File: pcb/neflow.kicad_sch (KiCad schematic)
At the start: 62 parts, among them J101 1333870, J102 FAN0, J103 SSR0, J104 FAN1, J105 SSR1, J106 Temp0, J107 Temp1, Q101 Q_PMOS_GSD, Q102 IRLML2502, Q103 IRLML2502, Q104 IRLML2502, Q105 IRLML2502, Q106 IRLML2502, SW101 SW_Push, SW102 SW_Push, SW103 SW_Push, SW104 SW_Push, U101 Pico, U102 TLV803EF29DBZR, U103 MAX31855KASA+T, U104 MAX31855KASA+T

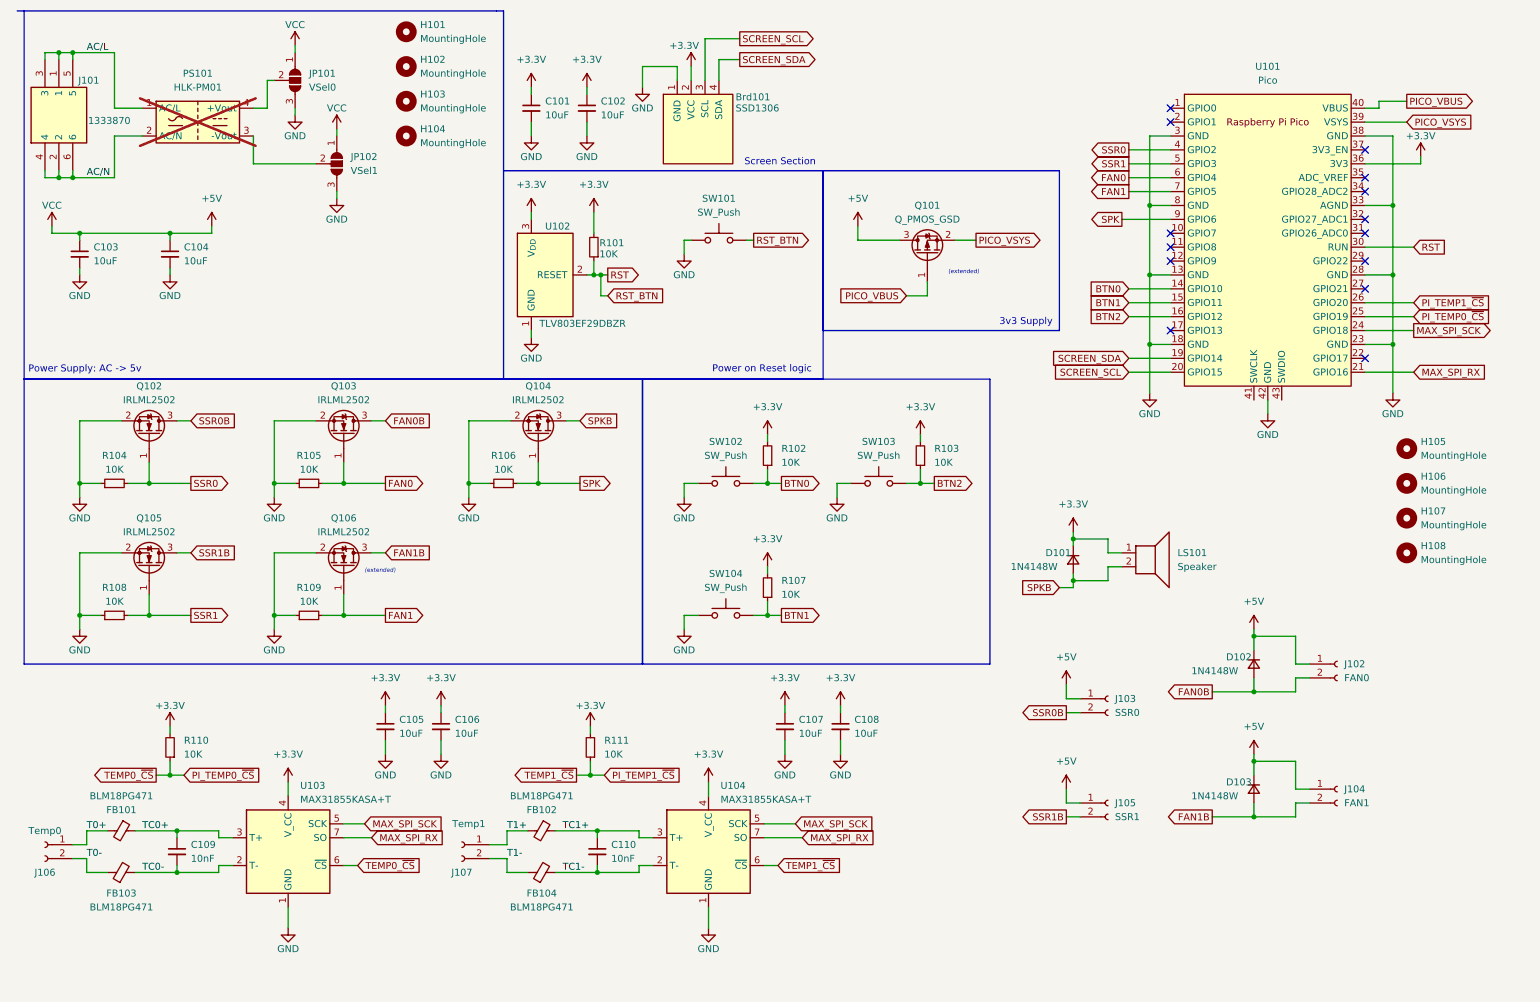
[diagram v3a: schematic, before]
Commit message: Reworking to rp2350 intergrated
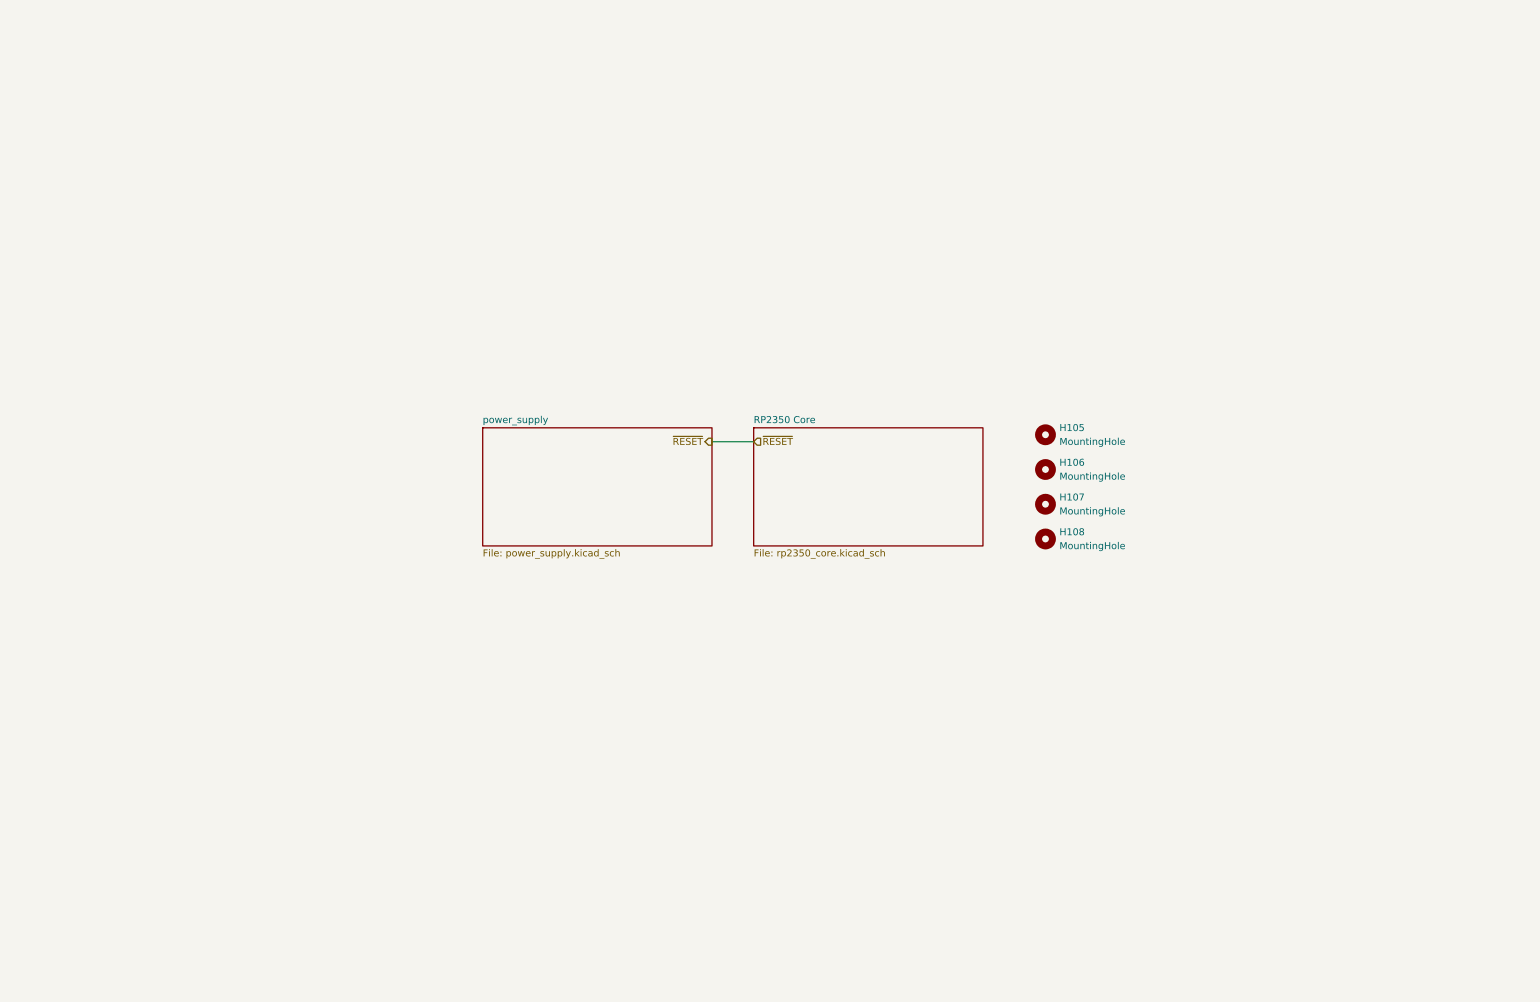
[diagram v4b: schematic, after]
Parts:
- removed Brd101: SSD1306, SSD1306:128x64OLED, symbol SSD1306-128x64_OLED:SSD1306
- removed C101, C102, C103, C104, C105, C106, C107, C108: 10uF, Resistor_SMD:R_0603_1608Metric, symbol Device:C_Small
- removed C109, C110: 10nF, Resistor_SMD:R_0603_1608Metric, symbol Device:C_Small
- removed D101, D102, D103: 1N4148W, Diode_SMD:D_SOD-123, symbol Device:D_Small
- removed FB101, FB102, FB103, FB104: BLM18PG471, Resistor_SMD:R_0603_1608Metric, symbol Device:FerriteBead_Small
- removed H101, H102, H103, H104: MountingHole, MountingHole:MountingHole_3mm, symbol Mechanical:MountingHole
- removed J101: 1333870, Unshareable:1333870, symbol 1333870:1333870
- removed J102: FAN0, Connector_JST:JST_XH_B2B-XH-AM_1x02_P2.50mm_Vertical, symbol Connector:Conn_01x02_Socket
- removed J103: SSR0, Connector_JST:JST_XH_B2B-XH-AM_1x02_P2.50mm_Vertical, symbol Connector:Conn_01x02_Socket
- removed J104: FAN1, Connector_JST:JST_XH_B2B-XH-AM_1x02_P2.50mm_Vertical, symbol Connector:Conn_01x02_Socket
- removed J105: SSR1, Connector_JST:JST_XH_B2B-XH-AM_1x02_P2.50mm_Vertical, symbol Connector:Conn_01x02_Socket
- removed J106: Temp0, Connector_JST:JST_XH_B2B-XH-AM_1x02_P2.50mm_Vertical, symbol Connector:Conn_01x02_Socket
- removed J107: Temp1, Connector_JST:JST_XH_B2B-XH-AM_1x02_P2.50mm_Vertical, symbol Connector:Conn_01x02_Socket
- removed JP101: VSel0, Jumper:SolderJumper-3_P1.3mm_Open_Pad1.0x1.5mm, symbol Jumper:SolderJumper_3_Open
- removed JP102: VSel1, Jumper:SolderJumper-3_P1.3mm_Open_Pad1.0x1.5mm, symbol Jumper:SolderJumper_3_Open
- removed LS101: Speaker, Library:PassiveBuzzerSMD_JiangsuHuaneng_MLT-5030, symbol Device:Speaker
- removed PS101: HLK-PM01, Converter_ACDC:Converter_ACDC_HiLink_HLK-PMxx, symbol Converter_ACDC:HLK-PM01
- removed Q101: Q_PMOS_GSD, Package_TO_SOT_SMD:SOT-23, symbol Device:Q_PMOS_GSD
- removed Q102, Q103, Q104, Q105, Q106: IRLML2502, Package_TO_SOT_SMD:SOT-23, symbol Transistor_FET:IRLML2060
- removed R101, R102, R103, R104, R105, R106, R107, R108, R109, R110, R111: 10K, Resistor_SMD:R_0603_1608Metric, symbol Device:R_Small
- removed SW101, SW102, SW103, SW104: SW_Push, silicone_btn:BUTTON_SILICON, symbol Switch:SW_Push
- removed U101: Pico, MCU_RaspberryPi_and_Boards:RPi_Pico_SMD_TH, symbol MCU_RaspberryPi_and_Boards:Pico
- removed U102: TLV803EF29DBZR, Package_TO_SOT_SMD:SOT-23, symbol Power_Supervisor:TLV810EA29DBZ
- removed U103, U104: MAX31855KASA+T, Package_SO:SOIC-8_3.9x4.9mm_P1.27mm, symbol Sensor_Temperature:MAX31855SASA
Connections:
- no-connect marks 14 -> 0
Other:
- added sheet RP2350 Core (rp2350_core.kicad_sch)
- added sheet power_supply (power_supply.kicad_sch)
- note removed: "(extended)"
- note removed: "3v3 Supply"
- note removed: "Power Supply: AC -> 5v"
- note removed: "Power on Reset logic"
- note removed: "Screen Section"
- moved on the sheet: H105, H106, H107, H108
